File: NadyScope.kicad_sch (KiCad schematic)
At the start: 0 parts

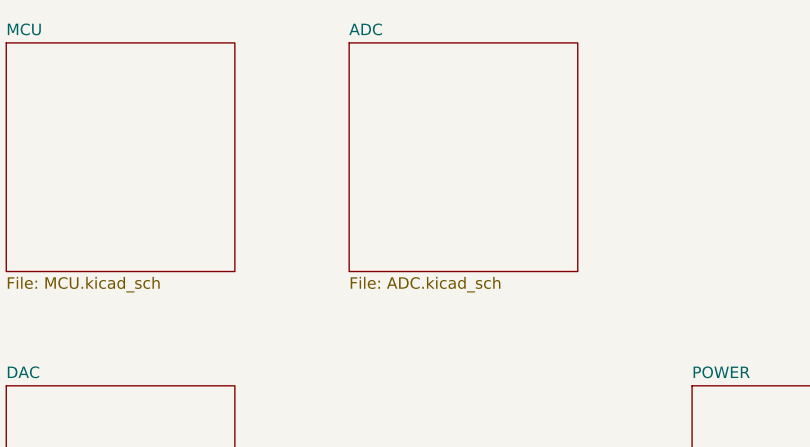
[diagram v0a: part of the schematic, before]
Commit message: finished ADC side, may add some additional bare channels, started DAC part and need to add the tca0372 amplifier or think about it
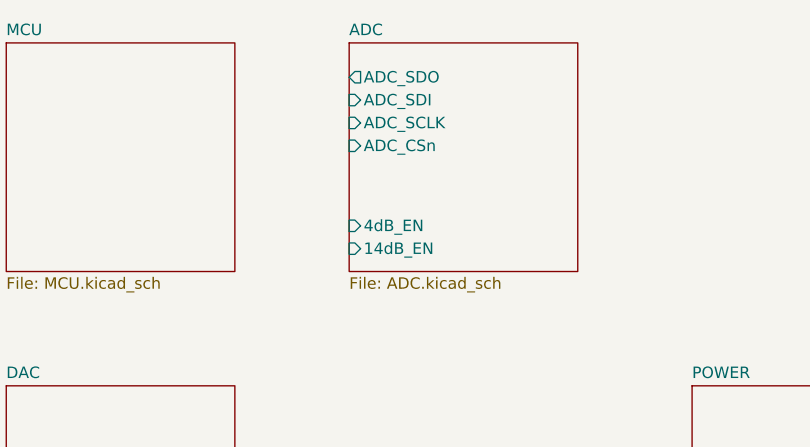
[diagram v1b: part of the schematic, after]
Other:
- sheet ADC ports: added 14dB_EN, 4dB_EN, ADC_CSn, ADC_SCLK, ADC_SDI, ADC_SDO; removed none
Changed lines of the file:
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@@
+			)
+		)
+		(pin "4dB_EN" input
+			(at 114.3 58.42 180)
+			(effects
+				(font
+					(size 1.27 1.27)
+				)
+				(justify left)
+			)
+		)
+		(pin "14dB_EN" input
+			(at 114.3 60.96 180)
+			(effects
+				(font
+					(size 1.27 1.27)
+				)
+				(justify left)
+			)
+		)
+		(pin "ADC_CSn" input
+			(at 114.3 49.53 180)
+			(effects
+				(font
+					(size 1.27 1.27)
+				)
+				(justify left)
+			)
+		)
+		(pin "ADC_SCLK" input
+			(at 114.3 46.99 180)
+			(effects
+				(font
+					(size 1.27 1.27)
+				)
+				(justify left)
+			)
+		)
+		(pin "ADC_SDI" input
+			(at 114.3 44.45 180)
+			(effects
+				(font
+					(size 1.27 1.27)
+				)
+				(justify left)
+			)
+		)
+		(pin "ADC_SDO" output
+			(at 114.3 41.91 180)
+			(effects
+				(font
+					(size 1.27 1.27)
+				)
+				(justify left)
 			)
 		)

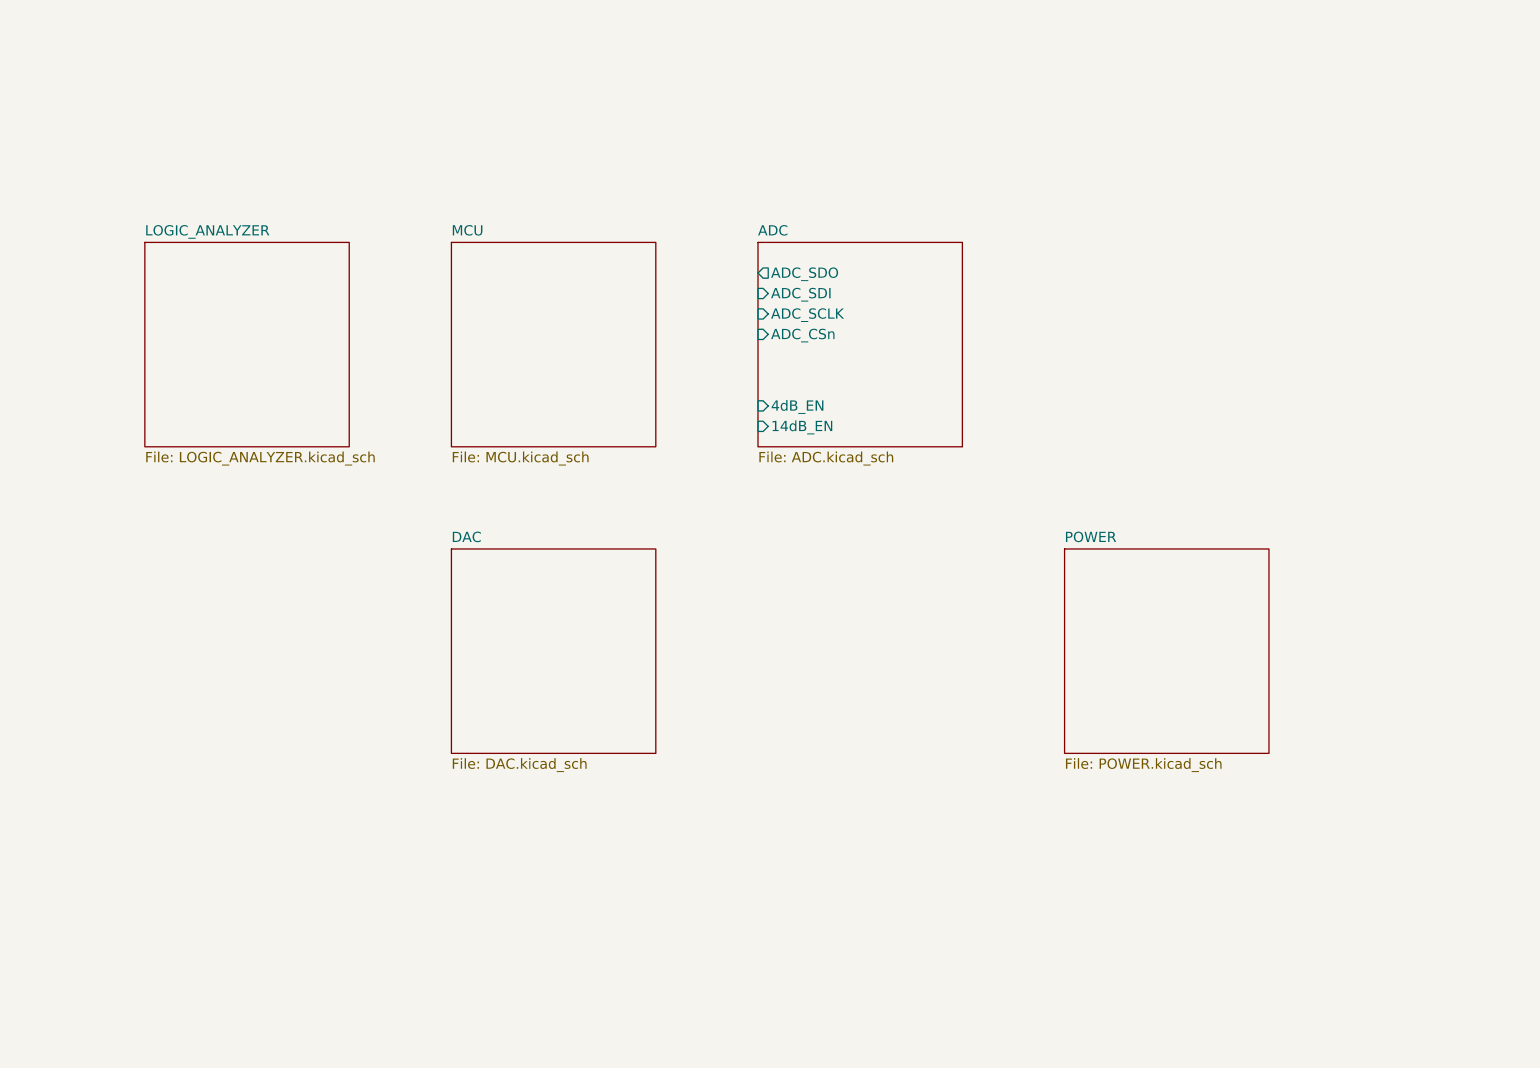
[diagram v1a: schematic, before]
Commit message: 80% done, maybe add more AINs, finish the power circuit and add system & block diagrams
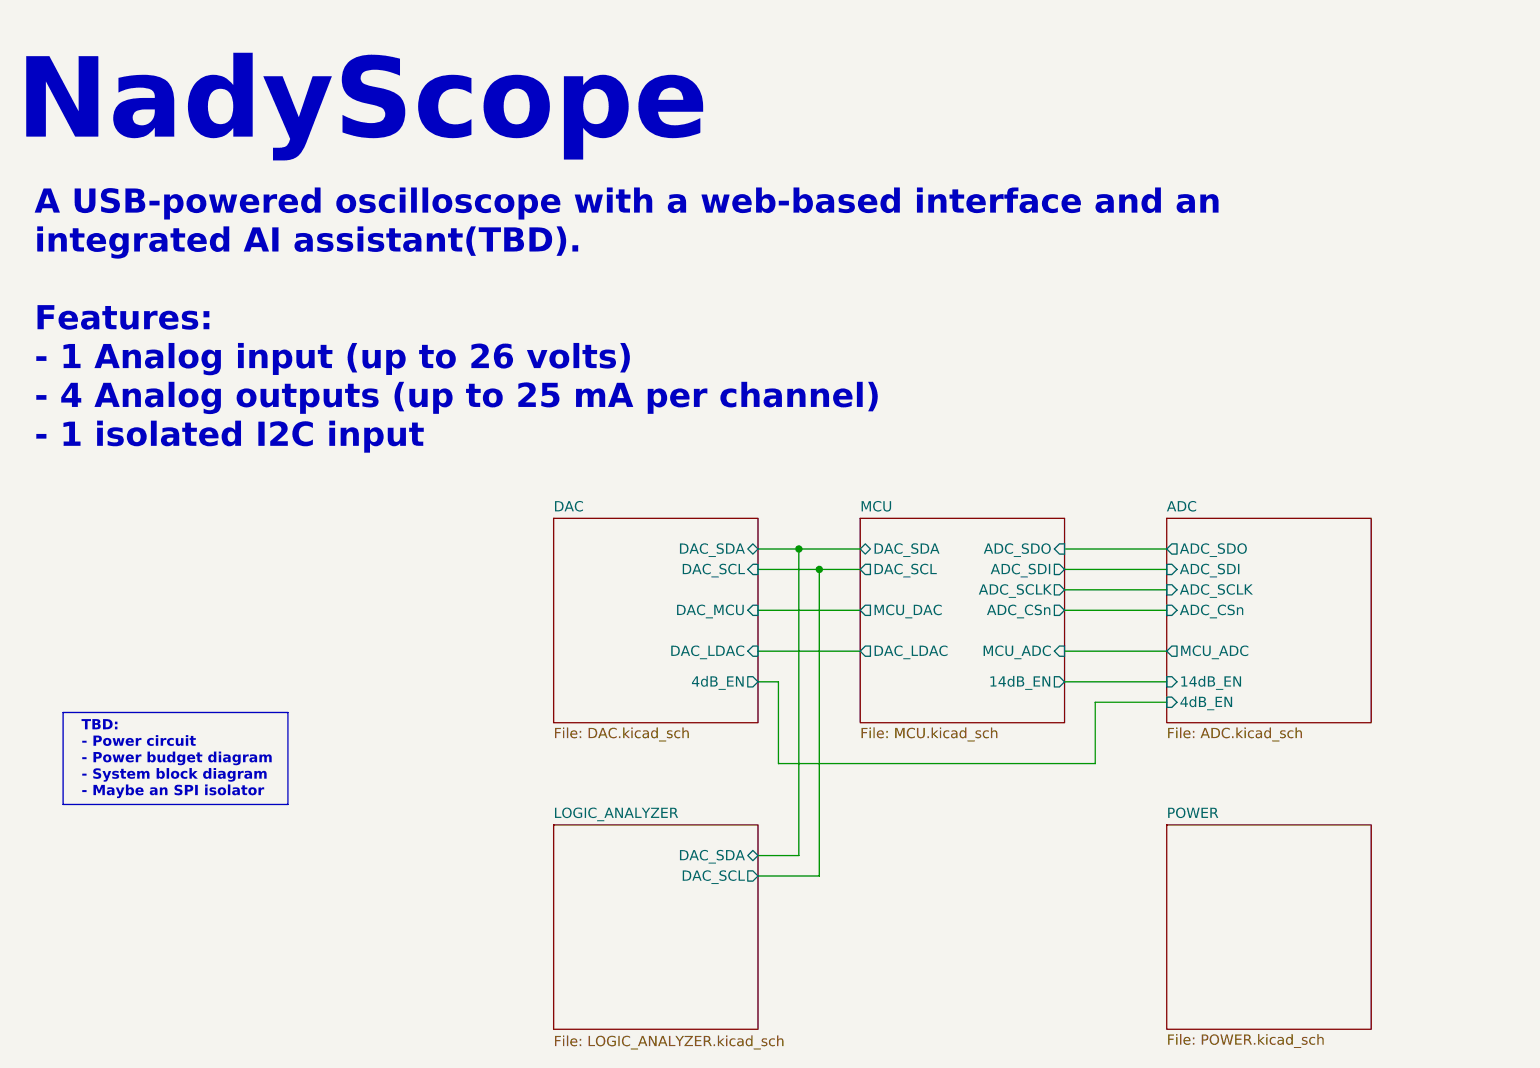
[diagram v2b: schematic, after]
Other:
- sheet ADC ports: added MCU_ADC; removed none
- sheet DAC ports: added 4dB_EN, DAC_LDAC, DAC_MCU, DAC_SCL, DAC_SDA; removed none
- sheet LOGIC_ANALYZER ports: added DAC_SCL, DAC_SDA; removed none
- sheet MCU ports: added 14dB_EN, ADC_CSn, ADC_SCLK, ADC_SDI, ADC_SDO, DAC_LDAC, DAC_SCL, DAC_SDA, MCU_ADC, MCU_DAC; removed none
- note added: "A USB-powered oscilloscope with a web-based interface and an integrated AI assistant(TBD). Features: - 1 Analog input (up to 26 volts) - 4 Analog outputs (up to 25 mA per channel) - 1 isolated I2C input"
- note added: "NadyScope"
- note added: "TBD: - Power circuit - Power budget diagram - System block diagram - Maybe an SPI isolator"

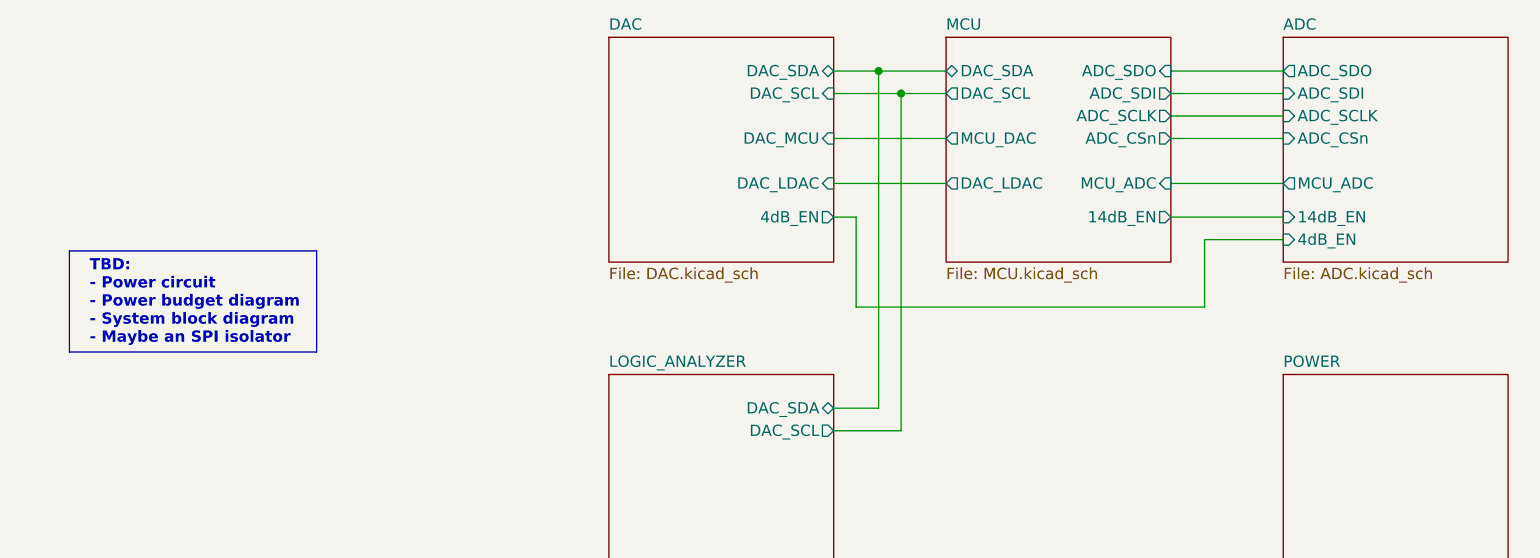
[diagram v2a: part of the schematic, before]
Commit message: finished individual block placement and started integrating, might need to change the AFEs length
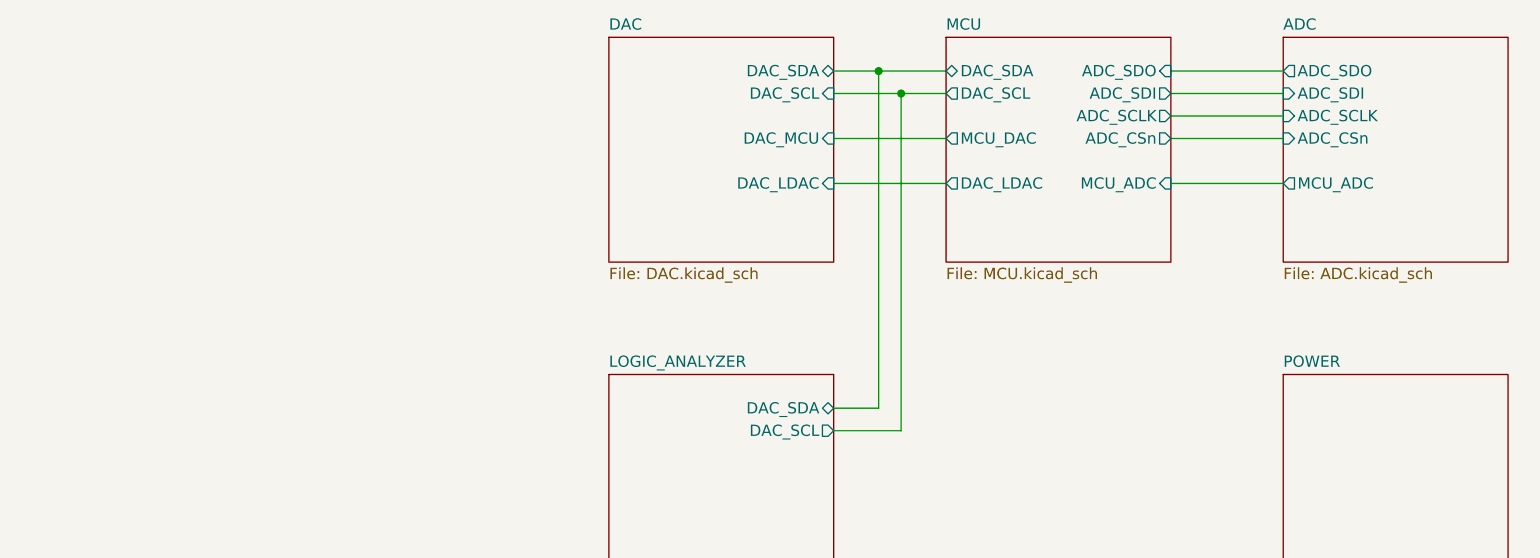
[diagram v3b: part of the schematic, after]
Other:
- sheet ADC ports: added none; removed 14dB_EN, 4dB_EN
- sheet DAC ports: added none; removed 4dB_EN
- sheet MCU ports: added none; removed 14dB_EN
- note removed: "TBD: - Power circuit - Power budget diagram - System block diagram - Maybe an SPI isolator"
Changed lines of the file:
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@@
 		(company "Elnady Electronics")
-	)
-	(rectangle
-		(start 27.94 96.52)
-		(end 55.88 107.95)
-		(stroke
-			(width 0)
-			(type default)
-		)
-		(fill
-			(type none)
-		)
 	)
 	(text "A USB-powered oscilloscope with a web-based interface and an\nintegrated AI assistant(TBD).\n\nFeatures:\n- 1 Analog input (up to 26 volts)\n- 4 Analog outputs (up to 25 mA per channel)\n- 1 isolated I2C input"
@@
 		)
 	)
-	(text "TBD:\n- Power circuit\n- Power budget diagram\n- System block diagram\n- Maybe an SPI isolator"
-		(exclude_from_sim no)
-		(at 30.226 102.362 0)
-		(effects
-			(font
-				(size 1.27 1.27)
-				(thickness 0.254)
-				(bold yes)
-			)
-			(justify left)
-		)
-	)
 	(text "NadyScope"
 		(exclude_from_sim no)
@@
 	(wire
 		(pts
-			(xy 156.21 102.87) (xy 156.21 95.25)
-		)
-		(stroke
-			(width 0)
-			(type default)
-		)
-	)
-	(wire
-		(pts
 			(xy 152.4 78.74) (xy 165.1 78.74)
 		)
@@
 	(wire
 		(pts
-			(xy 156.21 95.25) (xy 165.1 95.25)
-		)
-		(stroke
-			(width 0)
-			(type default)
-		)
-	)
-	(wire
-		(pts
 			(xy 121.92 78.74) (xy 127 78.74)
 		)
@@
 	(wire
 		(pts
-			(xy 116.84 102.87) (xy 156.21 102.87)
-		)
-		(stroke
-			(width 0)
-			(type default)
-		)
-	)
-	(wire
-		(pts
-			(xy 116.84 92.71) (xy 116.84 102.87)
-		)
-		(stroke
-			(width 0)
-			(type default)
-		)
-	)
-	(wire
-		(pts
 			(xy 152.4 88.9) (xy 165.1 88.9)
-		)
-		(stroke
-			(width 0)
-			(type default)
-		)
-	)
-	(wire
-		(pts
-			(xy 114.3 92.71) (xy 116.84 92.71)
-		)
-		(stroke
-			(width 0)
-			(type default)
-		)
-	)
-	(wire
-		(pts
-			(xy 152.4 92.71) (xy 165.1 92.71)
 		)
 		(stroke
@@
 			)
 		)
-		(pin "4dB_EN" output
-			(at 114.3 92.71 0)
-			(effects
-				(font
-					(size 1.27 1.27)
-				)
-				(justify right)
-			)
-		)
 		(instances
 			(project "NadyScope"
@@
 			)
 		)
-		(pin "4dB_EN" input
-			(at 165.1 95.25 180)
-			(effects
-				(font
-					(size 1.27 1.27)
-				)
-				(justify left)
-			)
-		)
-		(pin "14dB_EN" input
-			(at 165.1 92.71 180)
-			(effects
-				(font
-					(size 1.27 1.27)
-				)
-				(justify left)
-			)
-		)
 		(pin "ADC_CSn" input
 			(at 165.1 83.82 180)
@@
 			)
 		)
-		(pin "14dB_EN" output
-			(at 152.4 92.71 0)
-			(effects
-				(font
-					(size 1.27 1.27)
-				)
-				(justify right)
-			)
-		)

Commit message: DONE, ready for ordering
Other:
- note added: "A USB-powered oscilloscope/function generator/logic analyzer with a web-based interface and an integrated AI assistant(TBD)."
- note removed: "A USB-powered oscilloscope with a web-based interface and an integrated AI assistant(TBD). Features: - 1 Analog input (up to 26 volts) - 4 Analog outputs (up to 25 mA per channel) - 1 isolated I2C input"
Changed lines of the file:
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@@
 		(company "Elnady Electronics")
 	)
-	(text "A USB-powered oscilloscope with a web-based interface and an\nintegrated AI assistant(TBD).\n\nFeatures:\n- 1 Analog input (up to 26 volts)\n- 4 Analog outputs (up to 25 mA per channel)\n- 1 isolated I2C input"
+	(text "A USB-powered oscilloscope/function generator/logic analyzer\nwith a web-based interface and an integrated AI assistant(TBD).\n"
 		(exclude_from_sim no)
-		(at 24.384 47.752 0)
+		(at 24.384 34.036 0)
 		(effects
 			(font
